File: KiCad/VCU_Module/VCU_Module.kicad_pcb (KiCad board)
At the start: 4 copper layers, 85.2 x 107.8 mm, 66 parts, among them IC1 STM32C092RCT6, J1 5810132011, J10 12V, J11 Conn_ST_STDC14, J12 MCU1, J13 MCU2, J14 5V, J15 3V3, J16 MCU3, J17 MCU4, J2 CN1, J3 CN2, J4 CN3, J5 MCU6, J6 CN4, J7 MCU5, J8 Termination Resistor Jumper, J9 GND, Q1 SUD19P06-60, SW2 SW_Push, U3 LMR33640DDDA, U4 LMR33640DDDA, U6 MCP2562FDT-H_SN

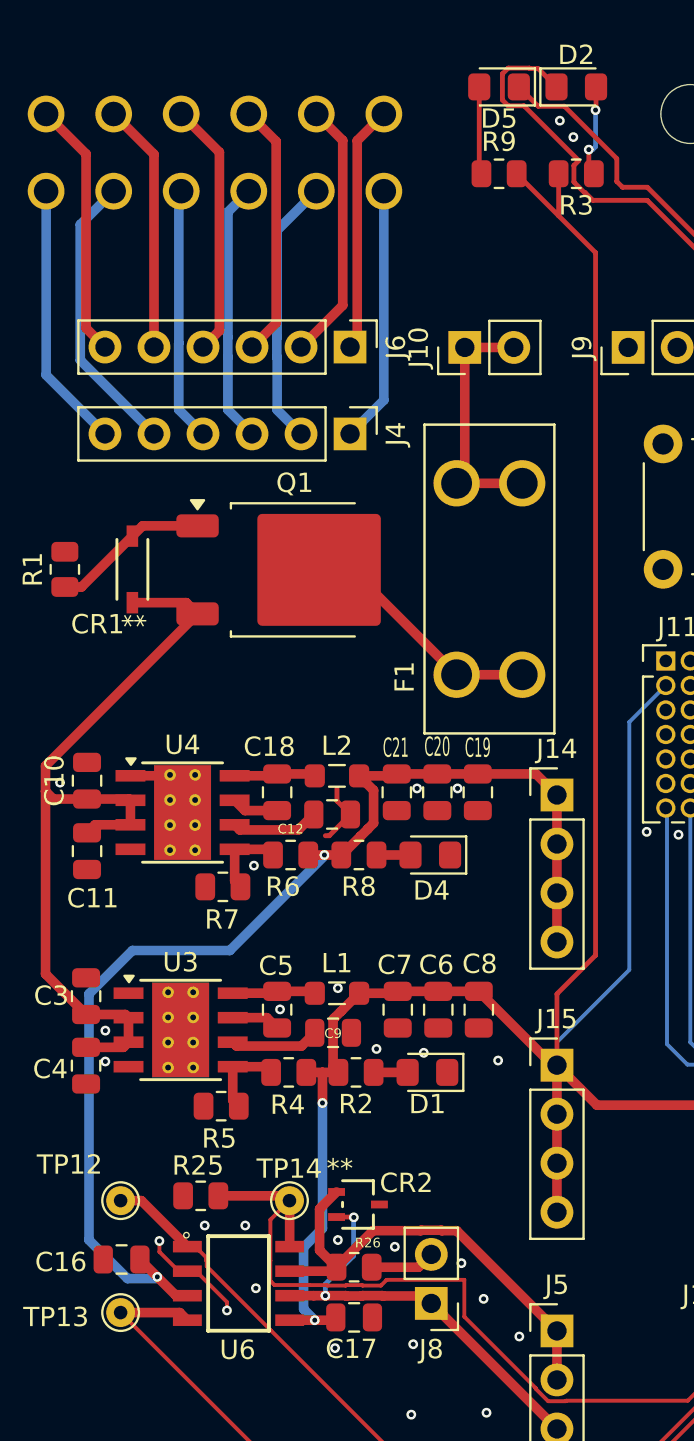
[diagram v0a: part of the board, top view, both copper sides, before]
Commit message: Clean up of libraries and some ERC and DRC fixes
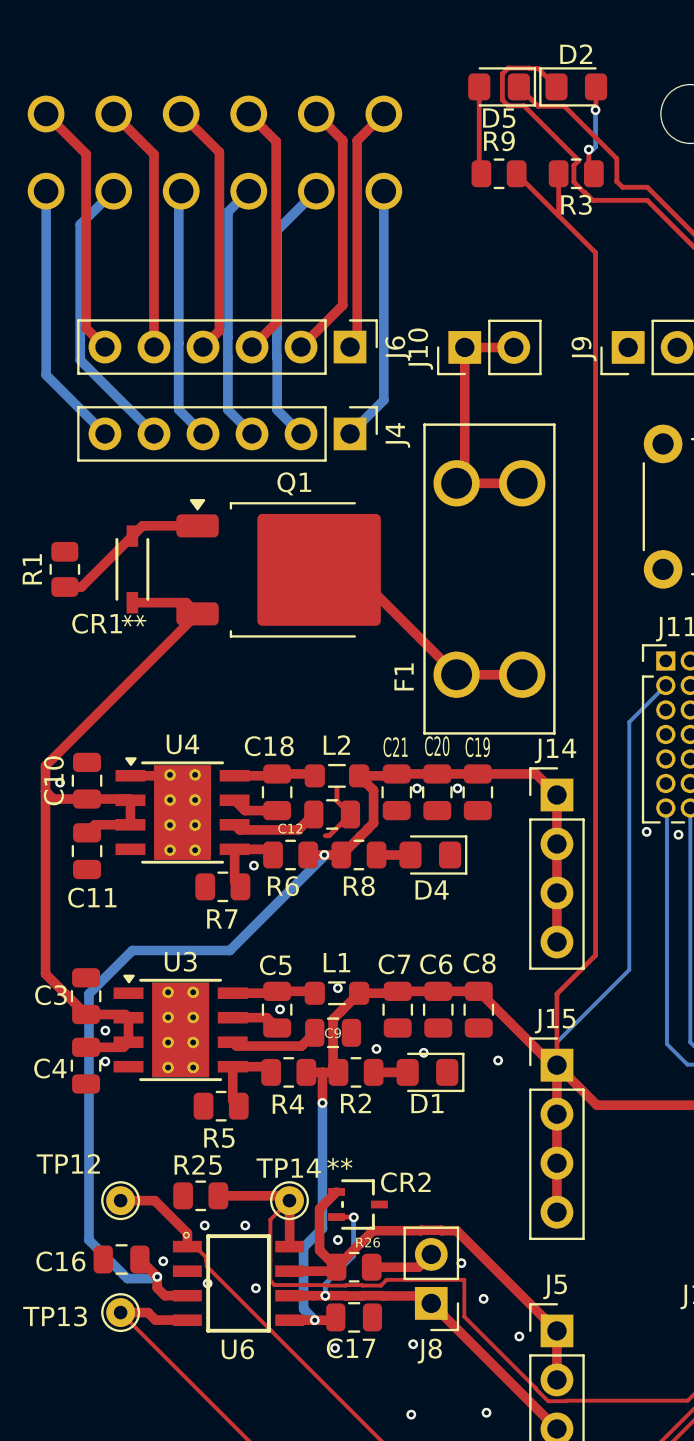
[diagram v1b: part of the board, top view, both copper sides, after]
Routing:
- net GND: track 12.0 -> 7.36 mm, vias 92 -> 89
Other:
- copper layers 4 -> 2

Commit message: final PCB fix
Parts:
- CR1: value MMSZ5240B -> MMSZ5245B-7-F
- CR3: footprint VMS_Footprints:ESDA051-1JY -> Diode_SMD:D_SOD-323
- D5: value GRN -> Amber
- R3: value 360 -> 1k
- R9: value 680 -> 1k
- moved R3 4.01 mm to (142.0, 62.5), turned to 0 degrees
- moved R9 3.99 mm to (146.0, 62.5), turned to 180 degrees
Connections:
- J11 pad 4: /MCU/SWDIO -> /MCU/SWCLK/BOOT0
- J11 pad 6: /MCU/SWCLK/BOOT0 -> /MCU/SWDIO
- R3 pad 1: Net-(D2-A) -> Net-(D5-A)
- R9 pad 1: Net-(D5-A) -> Net-(D2-A)
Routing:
- net GND: track 7.36 -> 3.01 mm, vias 89 -> 121
- net 3V3: track 149.4 -> 152.7 mm
- net /VIN_PROTECTED: track 42.6 -> 44.3 mm
- net 5V: track 61.1 -> 62.1 mm
- net /MCU/SWCLK/BOOT0: track 33.1 -> 34.1 mm
- net /MCU/CANH: track 24.1 -> 24.8 mm
- net Net-(Q1-G): track 8.19 -> 8.89 mm
- net /MCU/CANL: track 24.9 -> 25.5 mm
- net /MCU/SWDIO: track 35.6 -> 35.0 mm
